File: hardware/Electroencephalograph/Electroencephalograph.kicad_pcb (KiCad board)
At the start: 2 copper layers, 100 x 100 mm, 262 parts, among them J1 Conn_01x08_Male, J2 Conn_01x08_Male, U1 ADS1298IPAG, U2 OPA330xxD, U3 TMS320LF2406PZ, U4 THI3-0511, U5 ADUM2401BRWZ, U6 TPS60403, U7 LP5912-1.8DRVT, U8 LP5912-1.8DRVT, U9 LP5912-1.8DRVT

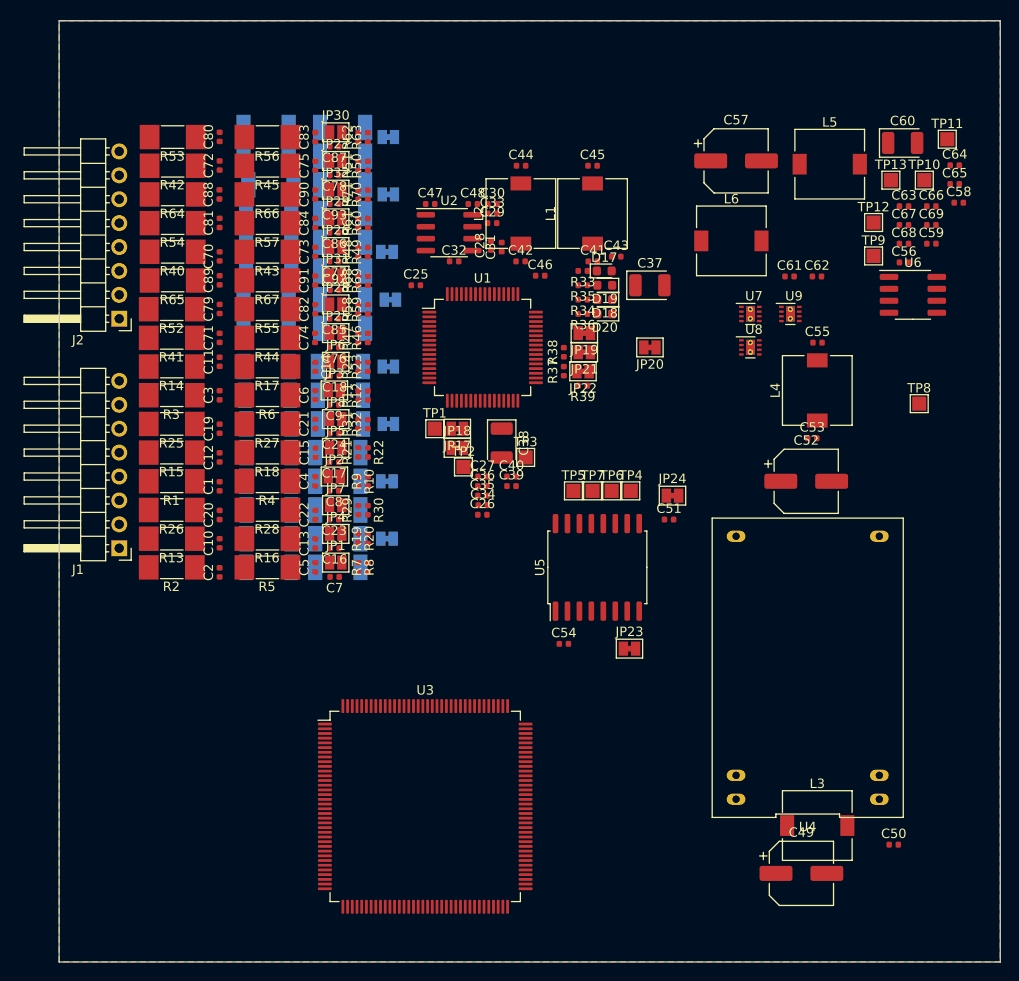
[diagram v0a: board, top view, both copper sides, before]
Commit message: placing power supply on pcb
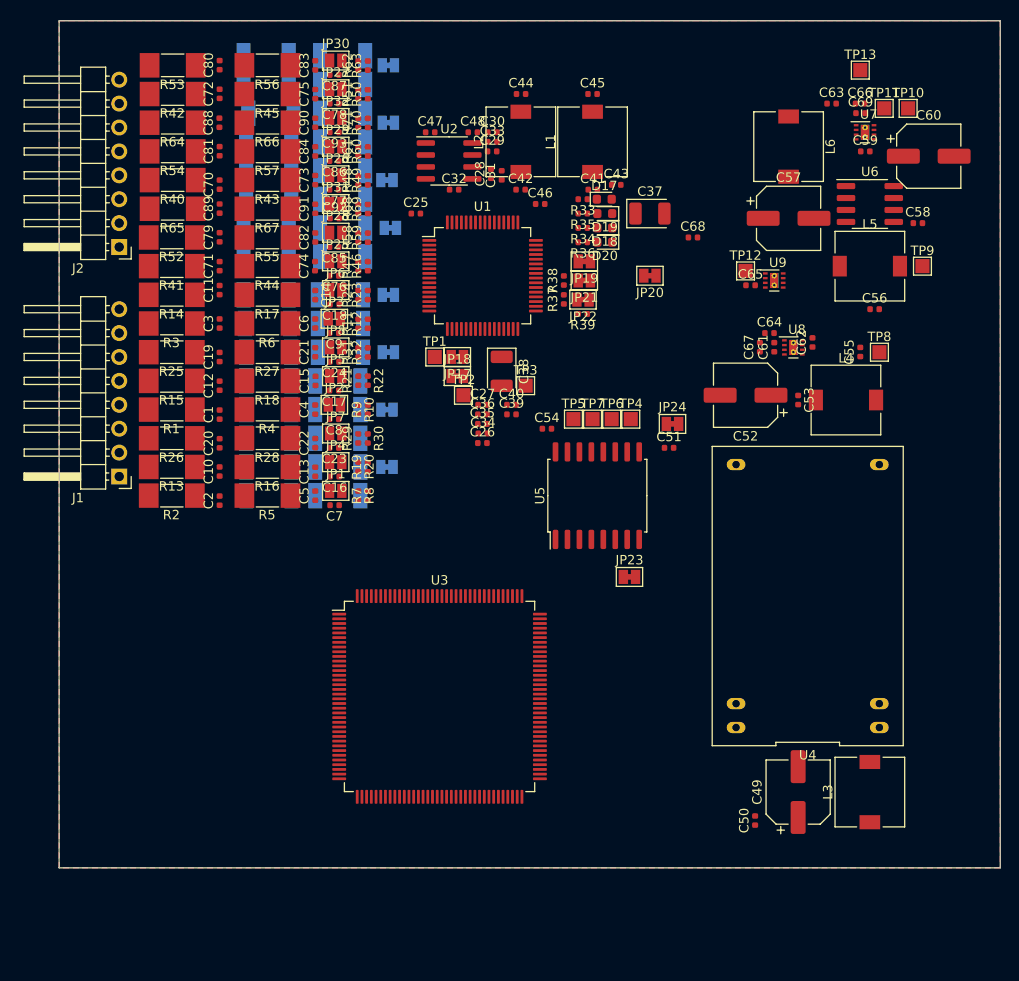
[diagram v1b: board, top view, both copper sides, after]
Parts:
- C60: footprint Capacitor_Tantalum_SMD:CP_EIA-3528-21_Kemet-B -> Capacitor_SMD:CP_Elec_6.3x5.8
- moved C64 26.6 mm to (125.5, 43.2)
- moved C65 24.2 mm to (123.5, 38.1)
- moved C54 22.9 mm to (101.8, 53.3)
- moved U7 22.8 mm to (135.6, 21.8)
- moved C68 22.4 mm to (117.3, 33.0)
- moved C67 20.1 mm to (124.5, 44.7), turned to 90 degrees
- moved C50 15.0 mm to (124.0, 95.0), turned to 90 degrees
- moved TP12 14.5 mm to (122.9, 36.6)
- moved C69 14.1 mm to (135.2, 19.8)
- moved C63 13.3 mm to (132.1, 18.8)
- moved C66 13.3 mm to (135.1, 18.8)
- moved TP13 12.1 mm to (135.1, 15.2)
- moved C59 12.1 mm to (135.7, 23.9)
- moved U3 11.8 mm to (90.4, 81.8)
- moved L6 11.7 mm to (127.5, 23.4), turned to 270 degrees
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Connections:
- C51 pad 1: VDDA -> Net-(C51-Pad1)
- JP23 pad 2: VDDA -> Net-(C51-Pad1)
- U5 pad 1: VDDA -> Net-(C51-Pad1)
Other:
- board size 100 x 100 mm -> 100 x 90 mm

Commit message: placing components groups
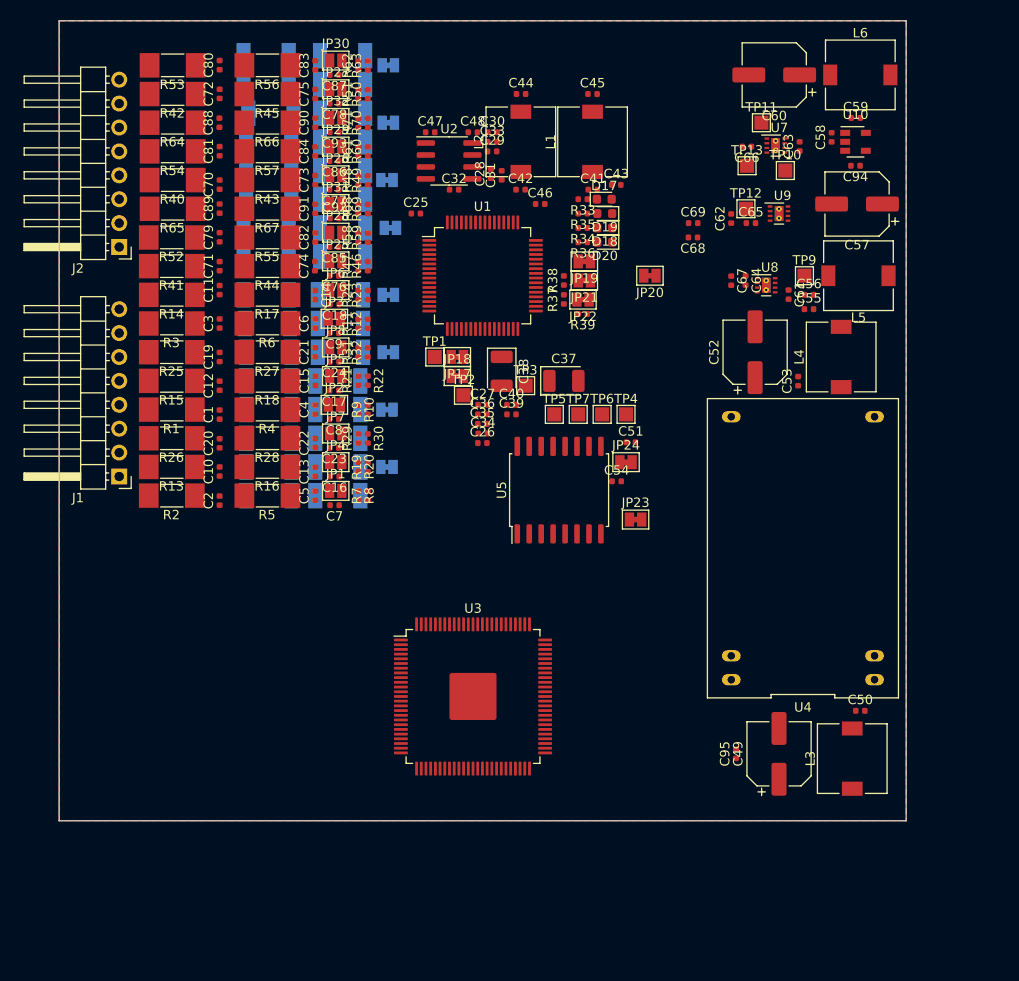
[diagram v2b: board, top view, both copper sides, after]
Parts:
- removed TP8: TestPoint, TestPoint:TestPoint_Pad_1.5x1.5mm
- removed U6: TPS60403, Package_SO:SOP-8_3.76x4.96mm_P1.27mm
- added C94: 1u, Capacitor_SMD:C_0402_1005Metric, F.Cu at (134.6, 25.4)
- added C95: 100n, Capacitor_SMD:C_0402_1005Metric, F.Cu at (121.9, 87.9)
- added U10: TPS60403, Package_TO_SOT_SMD:SOT-23-5, F.Cu at (134.6, 22.9)
- U3: value TMS320LF2406PZ -> DSPIC33FJ128MC710A; footprint Package_QFP:LQFP-144_20x20mm_P0.5mm -> Package_QFP:TQFP-100-1EP_14x14mm_P0.5mm_EP5x5mm
- moved C69 21.3 mm to (117.4, 31.5)
- moved C37 20.0 mm to (103.6, 48.3)
- moved C60 18.5 mm to (126.0, 15.7), turned to 180 degrees
- moved C50 16.2 mm to (135.1, 83.3), turned to 0 degrees
- moved TP13 15.7 mm to (123.1, 25.4)
- moved C62 15.7 mm to (121.4, 31.0)
- moved TP10 14.6 mm to (127.2, 25.9)
- moved TP11 13.1 mm to (124.6, 20.8)
- moved C58 12.9 mm to (132.1, 22.4), turned to 90 degrees
- moved C66 12.9 mm to (123.1, 23.4), turned to 180 degrees
- moved TP9 12.6 mm to (129.2, 37.1)
- moved L6 10.8 mm to (135.1, 15.7), turned to 0 degrees
- moved U7 9.60 mm to (126.1, 23.3)
- moved C54 9.28 mm to (109.2, 58.9)
- moved C67 7.70 mm to (121.4, 37.6), turned to 270 degrees
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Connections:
- C51 pad 1: Net-(C51-Pad1) -> VDDA
- C58 pad 1: (no net) -> Net-(C58-Pad1)
- JP23 pad 2: Net-(C51-Pad1) -> VDDA
- U3 pad 15: (no net) -> VSS
- U3 pad 36: (no net) -> VSS
- U3 pad 45: (no net) -> VSS
- U3 pad 65: (no net) -> VSS
- U3 pad 75: (no net) -> VSS
- U5 pad 1: Net-(C51-Pad1) -> VDDA
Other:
- board size 100 x 90 mm -> 90 x 85 mm

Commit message: fixed power supply symbols
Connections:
- C1 pad 2: GNDA -> A_GND
- C10 pad 2: GNDA -> A_GND
- C11 pad 2: GNDA -> A_GND
- C12 pad 2: GNDA -> A_GND
- C13 pad 2: GNDA -> A_GND
- C14 pad 2: GNDA -> A_GND
- C15 pad 2: GNDA -> A_GND
- C19 pad 2: GNDA -> A_GND
- C2 pad 2: GNDA -> A_GND
- C20 pad 2: GNDA -> A_GND
- C21 pad 2: GNDA -> A_GND
- C22 pad 2: GNDA -> A_GND
- C25 pad 2: VDDA -> A_VSS
- C26 pad 1: VDDA -> A_VDD
- C26 pad 2: GNDA -> A_GND
- C27 pad 1: VDDA -> A_VDD
- C27 pad 2: GNDA -> A_GND
- C28 pad 2: GNDA -> A_GND
- C29 pad 1: GNDA -> A_GND
- C29 pad 2: VDDA -> A_VDD
- C3 pad 2: GNDA -> A_GND
- C30 pad 1: GNDA -> A_GND
- C30 pad 2: VDDA -> A_VSS
- C31 pad 2: GNDA -> A_GND
- C32 pad 1: GNDA -> A_GND
- C32 pad 2: VDDA -> A_VDD
- C33 pad 1: GNDA -> A_GND
- C33 pad 2: VDDA -> A_VSS
- C34 pad 1: VDDA -> A_VSS
- C34 pad 2: GNDA -> A_GND
- C35 pad 1: VDDA -> A_VSS
- C35 pad 2: GNDA -> A_GND
- C36 pad 2: GNDA -> A_GND
- C37 pad 2: GNDA -> A_GND
- C38 pad 2: GNDA -> A_GND
- C39 pad 2: GNDA -> A_GND
- C4 pad 2: GNDA -> A_GND
- C40 pad 2: GNDA -> A_GND
- C41 pad 1: GNDA -> A_GND
- C42 pad 2: GNDA -> A_GND
- C43 pad 1: VDDA -> D_VDD
- C43 pad 2: GNDA -> A_GND
- C44 pad 1: GNDA -> A_GND
- C44 pad 2: VDDA -> A_VSS
- C45 pad 1: VDDA -> A_VDD
- C45 pad 2: GNDA -> A_GND
- C46 pad 1: VDDA -> D_VDD
- C46 pad 2: GNDA -> A_GND
- C47 pad 1: VDDA -> A_VDD
- C47 pad 2: GNDA -> A_GND
- C48 pad 1: VDDA -> A_VSS
- C48 pad 2: GNDA -> A_GND
- C49 pad 1: VDDA -> DP_VDD
- C49 pad 2: GNDA -> DP_GND
- C5 pad 2: GNDA -> A_GND
- C50 pad 2: GNDA -> DP_GND
- C51 pad 1: VDDA -> DP_VDD
- C51 pad 2: GNDA -> DP_GND
- C52 pad 2: GNDA -> A_GND
- C53 pad 2: GNDA -> A_GND
- C54 pad 1: VDDA -> D_VDD
- C54 pad 2: GNDA -> A_GND
- C55 pad 2: GNDA -> A_GND
- C56 pad 2: GNDA -> A_GND
- C57 pad 2: GNDA -> A_GND
- C59 pad 2: GNDA -> A_GND
- C6 pad 2: GNDA -> A_GND
- C60 pad 2: GNDA -> A_GND
- C61 pad 2: GNDA -> A_GND
- C62 pad 2: GNDA -> A_GND
- C63 pad 2: GNDA -> A_GND
- C64 pad 1: VDDA -> D_VDD
- C64 pad 2: GNDA -> A_GND
- C65 pad 1: VDDA -> A_VDD
- C65 pad 2: GNDA -> A_GND
- C66 pad 1: VDDA -> A_VSS
- C66 pad 2: GNDA -> A_GND
- C67 pad 1: VDDA -> D_VDD
- C67 pad 2: GNDA -> A_GND
- C68 pad 1: VDDA -> A_VDD
- C68 pad 2: VDDA -> A_VSS
- C69 pad 1: VDDA -> A_VDD
- C69 pad 2: VDDA -> A_VSS
- C70 pad 2: GNDA -> A_GND
- C71 pad 2: GNDA -> A_GND
- C72 pad 2: GNDA -> A_GND
- C73 pad 2: GNDA -> A_GND
- C74 pad 2: GNDA -> A_GND
- C75 pad 2: GNDA -> A_GND
- C79 pad 2: GNDA -> A_GND
- C80 pad 2: GNDA -> A_GND
- C81 pad 2: GNDA -> A_GND
- C82 pad 2: GNDA -> A_GND
- C83 pad 2: GNDA -> A_GND
- C84 pad 2: GNDA -> A_GND
- C88 pad 2: GNDA -> A_GND
- C89 pad 2: GNDA -> A_GND
- C90 pad 2: GNDA -> A_GND
- C91 pad 2: GNDA -> A_GND
- C94 pad 2: GNDA -> A_GND
- C95 pad 1: VDDA -> DP_VDD
- C95 pad 2: GNDA -> DP_GND
- D1 pad 1: VDDA -> A_VDD
- D10 pad 2: VDDA -> A_VSS
- D11 pad 1: VDDA -> A_VDD
- D12 pad 2: VDDA -> A_VSS
- D13 pad 1: VDDA -> A_VDD
- D14 pad 2: VDDA -> A_VSS
- D15 pad 1: VDDA -> A_VDD
- D16 pad 2: VDDA -> A_VSS
- D17 pad 1: GNDA -> A_GND
- D18 pad 1: GNDA -> A_GND
- D19 pad 1: GNDA -> A_GND
- D2 pad 2: VDDA -> A_VSS
- D20 pad 1: GNDA -> A_GND
- D21 pad 1: VDDA -> A_VDD
- D22 pad 2: VDDA -> A_VSS
- D23 pad 1: VDDA -> A_VDD
- D24 pad 2: VDDA -> A_VSS
- D25 pad 1: VDDA -> A_VDD
- D26 pad 2: VDDA -> A_VSS
- D27 pad 1: VDDA -> A_VDD
- D28 pad 2: VDDA -> A_VSS
- D29 pad 1: VDDA -> A_VDD
- D3 pad 1: VDDA -> A_VDD
- D30 pad 2: VDDA -> A_VSS
- D31 pad 1: VDDA -> A_VDD
- D32 pad 2: VDDA -> A_VSS
- D33 pad 1: VDDA -> A_VDD
- D34 pad 2: VDDA -> A_VSS
- D35 pad 1: VDDA -> A_VDD
- D36 pad 2: VDDA -> A_VSS
- D4 pad 2: VDDA -> A_VSS
- D5 pad 1: VDDA -> A_VDD
- D6 pad 2: VDDA -> A_VSS
- D7 pad 1: VDDA -> A_VDD
- D8 pad 2: VDDA -> A_VSS
- D9 pad 1: VDDA -> A_VDD
- JP17 pad 1: VDDA -> A_VDD
- JP19 pad 1: GNDA -> A_GND
- JP20 pad 1: VDDA -> D_VDD
- JP21 pad 1: VDDA -> D_VDD
- JP22 pad 1: VDDA -> D_VDD
- JP23 pad 2: VDDA -> DP_VDD
- JP24 pad 2: VDDA -> D_VDD
- L1 pad 2: VDDA -> A_VSS
- L2 pad 2: VDDA -> A_VDD
- L3 pad 1: VDDA -> DP_VDD
- R10 pad 1: VDDA -> A_VSS
- R11 pad 2: VDDA -> A_VDD
- R12 pad 1: VDDA -> A_VSS
- R19 pad 2: VDDA -> A_VDD
- R20 pad 1: VDDA -> A_VSS
- R21 pad 2: VDDA -> A_VDD
- R22 pad 1: VDDA -> A_VSS
- R23 pad 2: VDDA -> A_VDD
- R24 pad 1: VDDA -> A_VSS
- R29 pad 2: VDDA -> A_VDD
- R30 pad 1: VDDA -> A_VSS
- R31 pad 2: VDDA -> A_VDD
- R32 pad 1: VDDA -> A_VSS
- R37 pad 1: GNDA -> A_GND
- R38 pad 1: GNDA -> A_GND
- R39 pad 1: GNDA -> A_GND
- R46 pad 2: VDDA -> A_VDD
- R47 pad 1: VDDA -> A_VSS
- R48 pad 2: VDDA -> A_VDD
- R49 pad 1: VDDA -> A_VSS
- R50 pad 2: VDDA -> A_VDD
- R51 pad 1: VDDA -> A_VSS
- R58 pad 2: VDDA -> A_VDD
- R59 pad 1: VDDA -> A_VSS
- R60 pad 2: VDDA -> A_VDD
- R61 pad 1: VDDA -> A_VSS
- R62 pad 2: VDDA -> A_VDD
- R63 pad 1: VDDA -> A_VSS
- R68 pad 2: VDDA -> A_VDD
- R69 pad 1: VDDA -> A_VSS
- R7 pad 2: VDDA -> A_VDD
- R70 pad 2: VDDA -> A_VDD
- R71 pad 1: VDDA -> A_VSS
- R8 pad 1: VDDA -> A_VSS
- R9 pad 2: VDDA -> A_VDD
- TP11 pad 1: VDDA -> D_VDD
- TP12 pad 1: VDDA -> A_VDD
- TP13 pad 1: VDDA -> A_VSS
- U1 pad 19: VDDA -> A_VDD
- U1 pad 20: VDDA -> A_VSS
- U1 pad 21: VDDA -> A_VDD
- U1 pad 22: VDDA -> A_VDD
- U1 pad 23: VDDA -> A_VSS
- U1 pad 25: VDDA -> A_VSS
- U1 pad 32: VDDA -> A_VSS
- U1 pad 33: GNDA -> A_GND
- U1 pad 48: VDDA -> D_VDD
- U1 pad 49: GNDA -> A_GND
- U1 pad 50: VDDA -> D_VDD
- U1 pad 51: GNDA -> A_GND
- U1 pad 52: GNDA -> A_GND
- U1 pad 56: VDDA -> A_VDD
- U1 pad 57: VDDA -> A_VSS
- U1 pad 58: VDDA -> A_VSS
- U1 pad 59: VDDA -> A_VDD
- U10 pad 4: GNDA -> A_GND
- U2 pad 4: VDDA -> A_VSS
- U2 pad 7: VDDA -> A_VDD
- U4 pad 12: GNDA -> A_GND
- U4 pad 23: GNDA -> DP_GND
- U4 pad 24: GNDA -> DP_GND
- U5 pad 1: VDDA -> DP_VDD
- U5 pad 15: GNDA -> A_GND
- U5 pad 16: VDDA -> D_VDD
- U5 pad 2: GNDA -> DP_GND
- U5 pad 8: GNDA -> DP_GND
- U5 pad 9: GNDA -> A_GND
- U7 pad 1: VDDA -> A_VSS
- U7 pad 3: GNDA -> A_GND
- U7 pad 5: GNDA -> A_GND
- U7 pad 7: GNDA -> A_GND
- U8 pad 1: VDDA -> D_VDD
- U8 pad 3: GNDA -> A_GND
- U8 pad 5: GNDA -> A_GND
- U8 pad 7: GNDA -> A_GND
- U9 pad 1: VDDA -> A_VDD
- U9 pad 3: GNDA -> A_GND
- U9 pad 5: GNDA -> A_GND
- U9 pad 7: GNDA -> A_GND
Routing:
- added copper zone on F.Cu, net A_GND
- removed copper zone on F.Cu, net GNDA

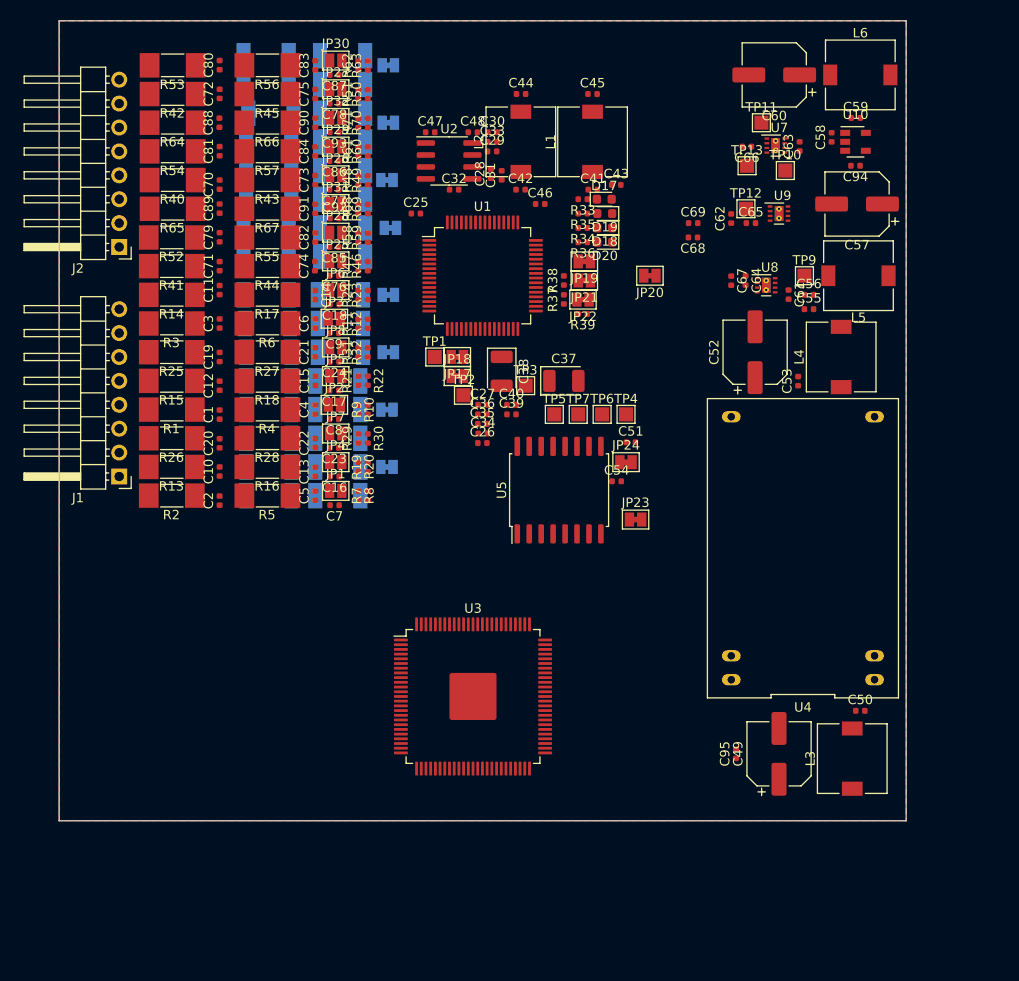
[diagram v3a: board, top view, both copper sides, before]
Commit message: fixed gnd clerance
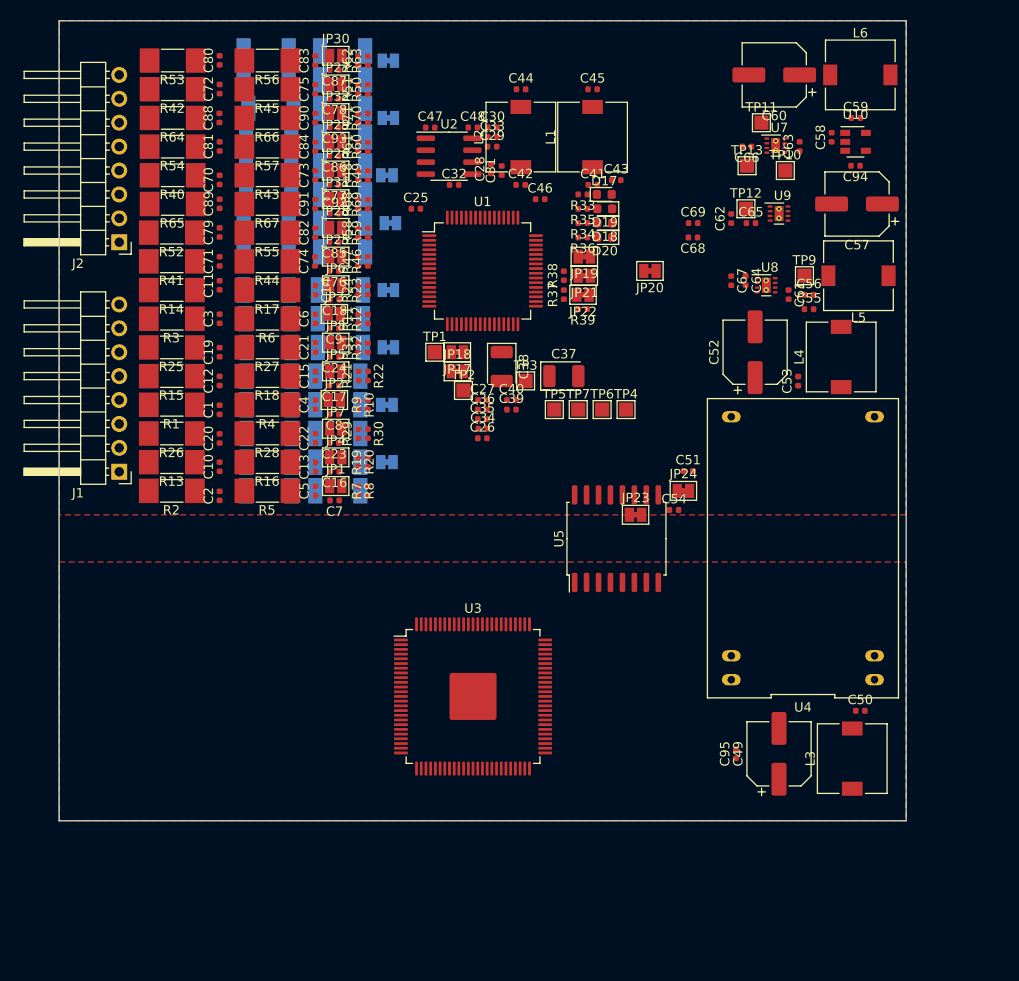
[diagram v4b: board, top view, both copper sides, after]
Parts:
- moved U5 7.99 mm to (109.2, 65.0)
- moved C51 6.82 mm to (116.8, 57.8)
- moved C54 6.82 mm to (115.3, 62.0)
- moved JP24 6.82 mm to (116.3, 59.9)
- moved C10 0.51 mm to (67.1, 57.4)
- moved C12 0.51 mm to (67.1, 48.3)
- moved C14 0.51 mm to (77.2, 38.6)
- moved C16 0.51 mm to (79.3, 57.9)
- moved C17 0.51 mm to (79.2, 48.8)
- moved C20 0.51 mm to (67.1, 54.4)
- moved C21 0.51 mm to (77.2, 44.7)
- moved C23 0.51 mm to (79.2, 54.9)
- moved C24 0.51 mm to (79.2, 45.7)
- moved C29 0.51 mm to (96.0, 23.4)
- moved C3 0.51 mm to (67.1, 41.7)
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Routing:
- added copper zone on F.Cu, net DP_GND
